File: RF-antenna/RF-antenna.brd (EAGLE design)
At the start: 108.2 x 108.2 mm, 15 parts, among them CON1 UMC_CONNECTORREGULAR, CON2 UMC_CONNECTORREGULAR, U3 THS3091DDAR

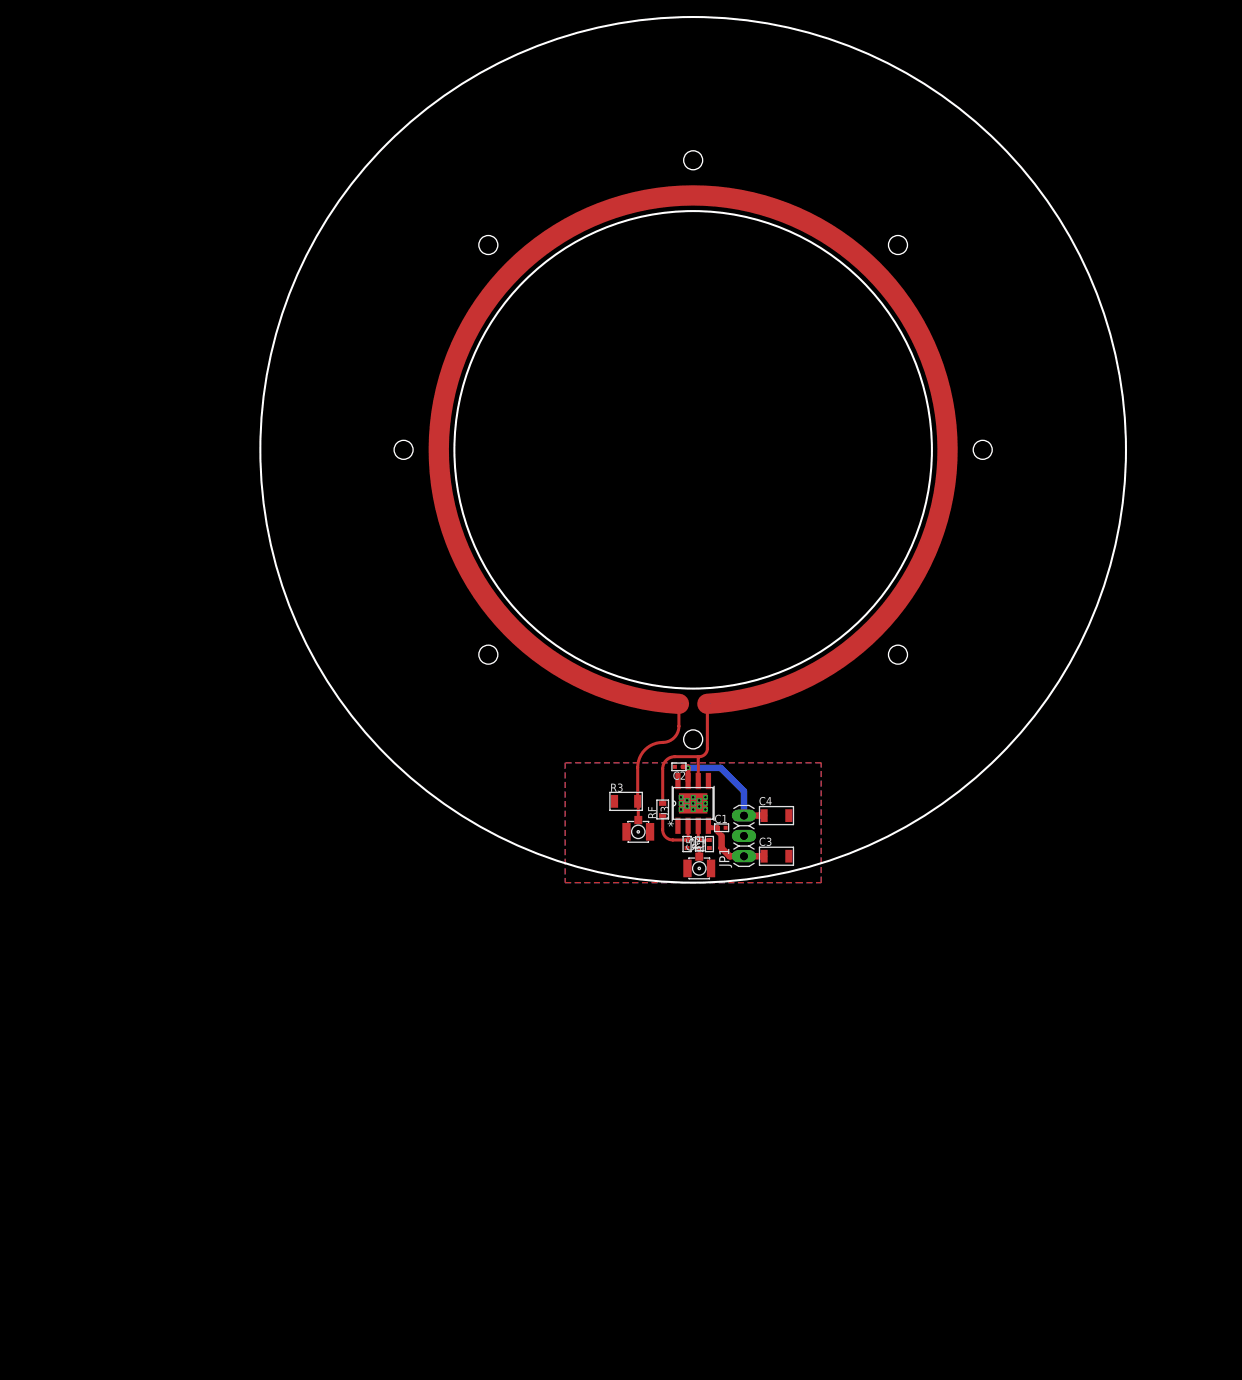
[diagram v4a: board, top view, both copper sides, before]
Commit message: Starting full board layout
Got the VtoI converter designed and have started laying out the RF antennas.

DSB
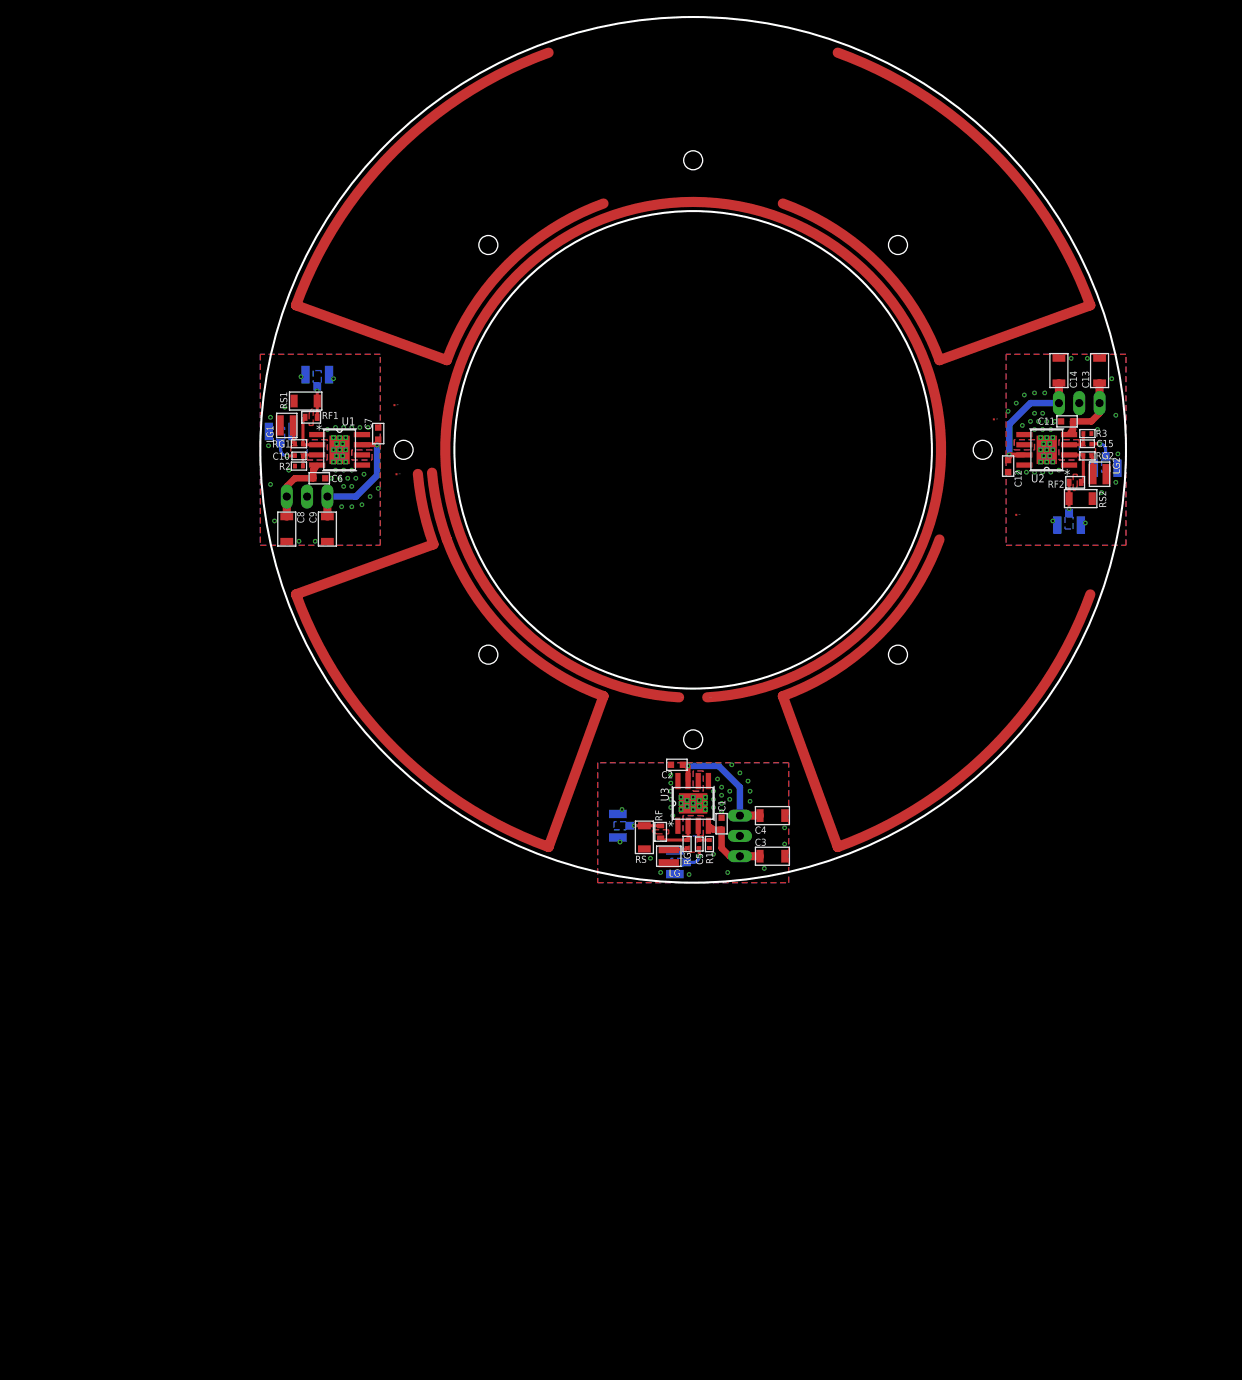
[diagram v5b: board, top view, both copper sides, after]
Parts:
- added C10, C15: 10nF, jqi_passives:C_MLCC_0402
- added C11, C12, C6, C7: 100nF, jqi_passives:C_MLCC_0603
- added C13, C14, C8, C9: 10uF, jqi_passives:C_MLCC_1206
- added CON3, CON4, CON5, CON6: UMC_CONNECTORREGULAR, qkdlab_alessandro:UMC_CONNECTOR
- added JP2, JP3: (no value), pinhead:1X03
- added LG, LG1, LG2: (no value), jqi_passives:1008
- added LW3, LW4, LW5, LW6: LITZ_TERM, RFantenna:LITZ_100MHZ
- added RF1, RF2: 866, jqi_passives:R_0603
- added RG, RG1, RG2: 95.3, jqi_passives:R_0402
- added RS, RS1, RS2: 10, jqi_passives:R_1206
- added U1, U2: THS3091DDAR, opamp-jqi:DDA8_2P28X2P28
- C1, C2: device jqi_passives:C_MLCC_0402 -> jqi_passives:C_MLCC_0603
- C5: value 22pF -> 10nF
- R1: value 50 -> 49.9
- R2: value 95.3 -> 49.9
- R3: value 4.99 -> 49.9; device jqi_passives:R_1206 -> jqi_passives:R_0402
- moved R3 73.7 mm to (103.4, 56.1), turned to 180 degrees
- moved R2 67.7 mm to (4.83, 52.1), turned to 0 degrees
- moved CON2 3.14 mm to (51.8, 2.54), flipped to the bottom, turned to 180 degrees
- moved RF 2.81 mm to (50.0, 6.35)
- moved CON1 2.65 mm to (44.7, 7.11), flipped to the bottom, turned to 180 degrees
- moved LW1 0.76 mm to (55.9, 23.1)
- moved LW2 0.76 mm to (52.3, 23.1)
- moved C3 0.51 mm to (64.0, 3.30)
- moved C4 0.51 mm to (64.0, 8.38)
- moved C1 0.51 mm to (57.7, 7.37), turned to 90 degrees
- moved JP1 0.51 mm to (59.9, 5.84), flipped to the bottom
- moved C2 0.36 mm to (52.1, 14.7)
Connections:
- new net D1_COIL: CON4.P$1, LW3.T1, LW4.T1, RF1.P$2, RS1.P$2, U1.6
- new net D2_COIL: CON6.P$1, LW5.T1, LW6.T1, RF2.P$2, RS2.P$2, U2.6
- new net N$10: LG1.P$2, RG1.P$2
- new net N$11: RF2.P$1, RG2.P$1, U2.2
- new net N$12: C15.P$2, R3.P$2, U2.3
- new net N$13: C15.P$1, CON5.P$1
- new net N$15: LG2.P$2, RG2.P$2
- new net N$6: LG.P$2, RG.P$2
- new net N$7: C10.P$2, R2.P$2, U1.3
- new net N$8: C10.P$1, CON3.P$1
- new net R_COIL: CON1.P$1, LW1.T1, LW2.T1, RF.P$2, RS.P$2, U3.6
- net +15V: now also C12.P$1, C14.P$1, C7.P$1, C9.P$1, JP2.3, JP3.3, U1.7, U2.7
- net -15V: now also C11.P$1, C13.P$1, C6.P$1, C8.P$1, JP2.1, JP3.1, U1.4, U2.4
- net GND: now also C11.P$2, C12.P$2, C13.P$2, C14.P$2, C6.P$2, C7.P$2, C8.P$2, C9.P$2, CON3.P$2, CON3.P$3, CON4.P$2, CON4.P$3, CON5.P$2, CON5.P$3, CON6.P$2, CON6.P$3, JP2.2, JP3.2, LG.P$1, LG1.P$1, LG2.P$1, R2.P$1, RS.P$1, RS1.P$1, RS2.P$1, U1.1, U1.5, U1.8, U1.EPAD, U1.P$1, U1.P$10, U1.P$11, U1.P$12, U1.P$13, U1.P$2, U1.P$3, U1.P$4, U1.P$5, U1.P$6, U1.P$7, U1.P$8, U1.P$9, U2.1, U2.5, U2.8, U2.EPAD, U2.P$1, U2.P$10, U2.P$11, U2.P$12, U2.P$13, U2.P$2, U2.P$3, U2.P$4, U2.P$5, U2.P$6, U2.P$7, U2.P$8, U2.P$9; no longer R2.P$2
- net N$1: now also RG.P$1; no longer R2.P$1
- net N$5: now also RF1.P$1, RG1.P$1, U1.2; no longer CON1.P$1, LW1.T1, LW2.T1, R3.P$2, RF.P$2, U3.6
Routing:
- net D1_COIL: track 0.00 -> 225.0 mm, vias 0 -> 1
- net D2_COIL: track 0.00 -> 189.2 mm, vias 0 -> 1
- net N$5: track 39.9 -> 5.27 mm
- net +15V: track 16.2 -> 49.1 mm, vias 1 -> 3
- net -15V: track 9.73 -> 28.1 mm
- net R_COIL: track 0.00 -> 7.86 mm, vias 0 -> 1
- net N$11: track 0.00 -> 5.27 mm
- net N$7: track 0.00 -> 3.12 mm
- net N$12: track 0.00 -> 3.12 mm
- net N$8: track 0.00 -> 2.91 mm, vias 0 -> 1
- net N$13: track 0.00 -> 2.91 mm, vias 0 -> 1
- net N$15: track 0.00 -> 2.35 mm
- net N$6: track 0.00 -> 2.35 mm
- net N$10: track 0.00 -> 2.35 mm
- net N$1: track 7.21 -> 5.27 mm
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
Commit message: Finished 1st order prototype
Ready to discuss with Alessandro and Steve. Rough estimate that one board will generate 20 kHz Rabi frequencies with the circular coil.

DSB
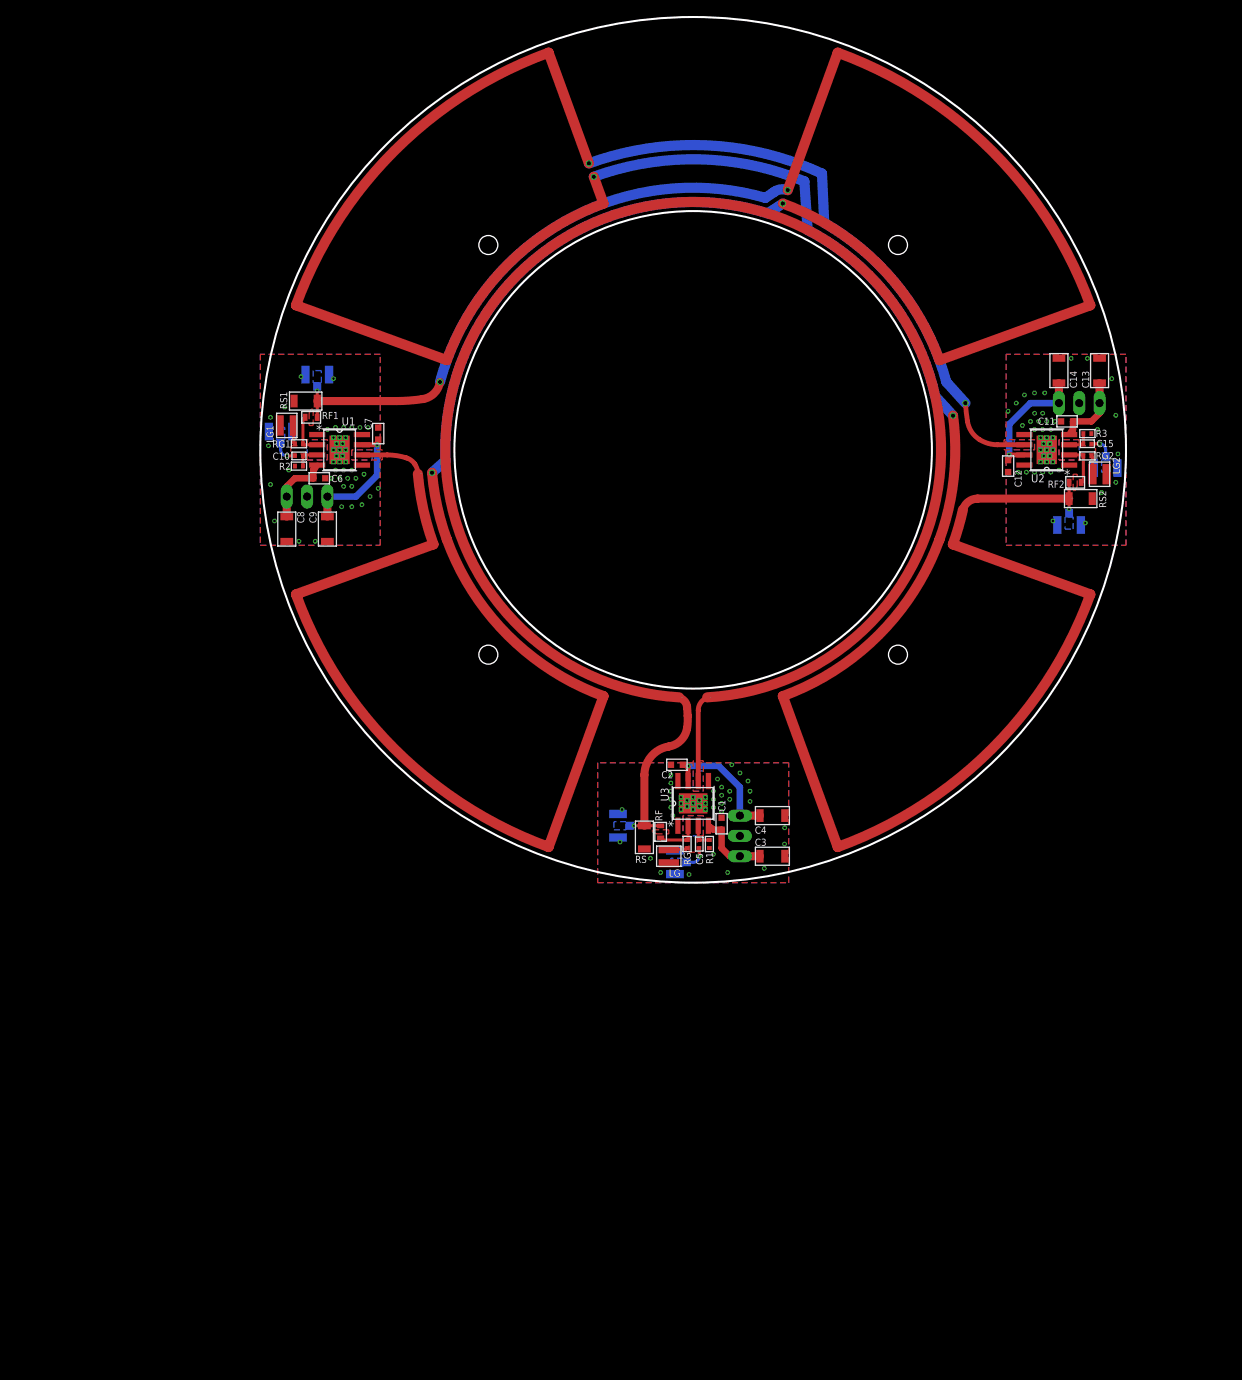
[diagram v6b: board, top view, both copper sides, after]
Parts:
- moved LW4 9.67 mm to (7.11, 60.2)
- moved LW6 6.91 mm to (101.1, 48.0)
- moved LW5 4.10 mm to (88.1, 59.9)
- moved LW3 2.67 mm to (19.7, 51.1)
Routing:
- net D2_COIL: track 189.2 -> 396.2 mm, vias 1 -> 5
- net D1_COIL: track 225.0 -> 372.8 mm, vias 1 -> 5
- net R_COIL: track 7.86 -> 37.1 mm
